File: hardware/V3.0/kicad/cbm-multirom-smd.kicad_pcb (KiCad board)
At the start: 2 copper layers, 26.1 x 63 mm, 27 parts, among them Con1 Signal, IC1 SST39SF0x0, IC2 328P(B), IC3 74HCT273, IC4 74HCT1G04, Q1 20MHz

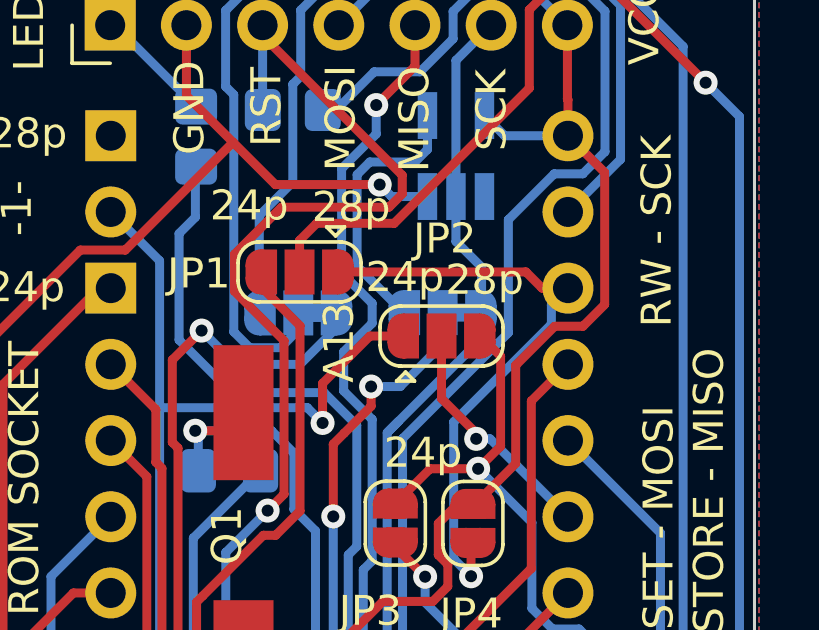
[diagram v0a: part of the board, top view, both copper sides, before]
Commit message: V3.0
Changed Jumper setup
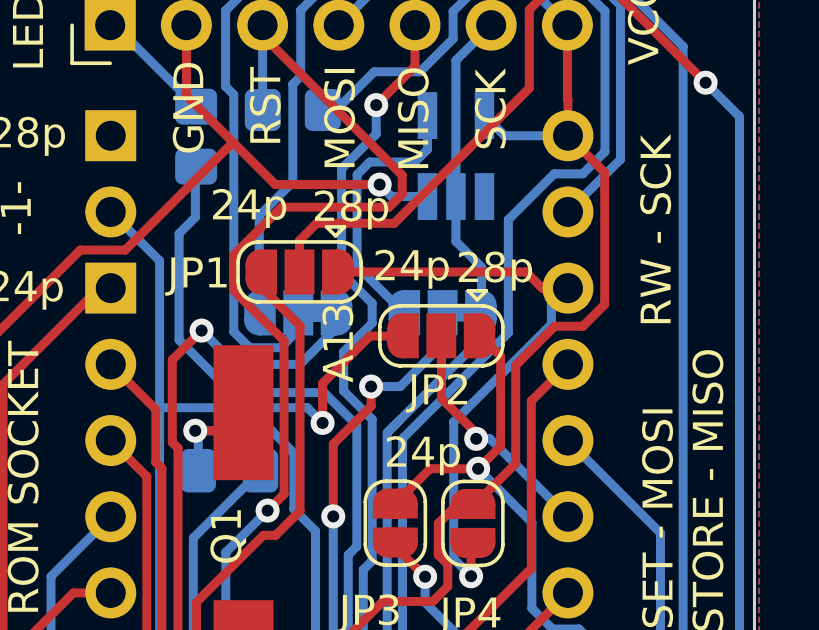
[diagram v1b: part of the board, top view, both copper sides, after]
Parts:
- turned JP2 to 180 degrees
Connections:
- JP2 pad 1: A12 -> A11
- JP2 pad 3: A11 -> A12
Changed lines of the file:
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@@
   )
   (footprint "Jumper:SolderJumper-3_P1.3mm_Open_RoundedPad1.0x1.5mm" (layer "F.Cu")
-    (at 138.39 87.6505)
+    (at 138.384 87.642 180)
     (descr "SMD Solder 3-pad Jumper, 1x1.5mm rounded Pads, 0.3mm gap, open")
     (tags "solder jumper open")
@@
     (property "ki_keywords" "Solder Jumper SPDT")
     (attr exclude_from_pos_files)
-    (fp_text reference "JP2" (at 0.107 -3.2485) (layer "F.SilkS")
+    (fp_text reference "JP2" (at 0.06 -1.822) (layer "F.SilkS")
         (effects (font (size 1 1) (thickness 0.15)))
     )
-    (fp_text value "28p" (at 1.436 -1.8745 180) (layer "F.SilkS")
+    (fp_text value "28p" (at -1.792 2.256) (layer "F.SilkS")
         (effects (font (size 1 1) (thickness 0.15)))
     )
-    (fp_text user "24p" (at -1.222 -1.9645 unlocked) (layer "F.SilkS")
+    (fp_text user "24p" (at 0.986 2.315 unlocked) (layer "F.SilkS")
         (effects (font (size 1 1) (thickness 0.15)))
     )
@@
     (fp_line (start 2.3 1.25) (end 2.3 -1.25)
       (stroke (width 0.05) (type solid)) (layer "F.CrtYd"))
-    (pad "1" smd custom (at -1.3 0) (size 1 0.5) (layers "F.Cu" "F.Mask")
-      (net 35 "A12") (pinfunction "A") (pintype "passive") (zone_connect 2) (thermal_bridge_angle 45)
+    (pad "1" smd custom (at -1.3 0 180) (size 1 0.5) (layers "F.Cu" "F.Mask")
+      (net 37 "A11") (pinfunction "A") (pintype "passive") (zone_connect 2) (thermal_bridge_angle 45)
       (options (clearance outline) (anchor rect))
       (primitives
@@
           (width 0) (fill yes))
       ))
-    (pad "2" smd rect (at 0 0) (size 1 1.5) (layers "F.Cu" "F.Mask")
+    (pad "2" smd rect (at 0 0 180) (size 1 1.5) (layers "F.Cu" "F.Mask")
       (net 53 "A11_A12") (pinfunction "C") (pintype "passive"))
-    (pad "3" smd custom (at 1.3 0) (size 1 0.5) (layers "F.Cu" "F.Mask")
-      (net 37 "A11") (pinfunction "B") (pintype "passive") (zone_connect 2) (thermal_bridge_angle 45)
+    (pad "3" smd custom (at 1.3 0 180) (size 1 0.5) (layers "F.Cu" "F.Mask")
+      (net 35 "A12") (pinfunction "B") (pintype "passive") (zone_connect 2) (thermal_bridge_angle 45)
       (options (clearance outline) (anchor rect))
       (primitives
